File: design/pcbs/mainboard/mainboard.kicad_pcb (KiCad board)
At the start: 4 copper layers, 150 x 130 mm, 253 parts, among them J1 Conn_Coaxial, J10 Conn_01x04, J11 Conn_01x04, J15 Conn_01x01, J16 Conn_01x01, J17 Conn_01x01, J18 Conn_01x01, J2 Conn_Coaxial, J4 AudioJackSw, J5 Conn_01x03, K1 EC2-5NU, K2 EC2-5NU, K3 EC2-12NU, K4 EC2-12NU, Q1 SS8050, Q10 SS8050, Q11 SS8050, Q12 SS8050, Q2 SS8050, Q3 SS8050, Q4 SS8050, Q5 SS8550, Q6 SS8550, Q7 SS8050, Q8 SS8050, Q9 SS8050, U1 TPS79318-EP, U10 TPS7A49, U11 PCM1792A, U12 OPA1612AxD, U13 OPA1612AxD, U14 OPA1612AxD, U15 KC3225K24.5760C1GE00, U16 5PB1102, U17 STM8S003F3P, U18 Combo384, U19 TPS7A49, U2 SRC4392, U20 TPS7A30, U3 TLV1117-33, U4 TPS7A49, U5 TPS7A30, U6 Si8645BA-B-IU, U7 OPA1612AxD, U8 LME49600, U9 LME49600

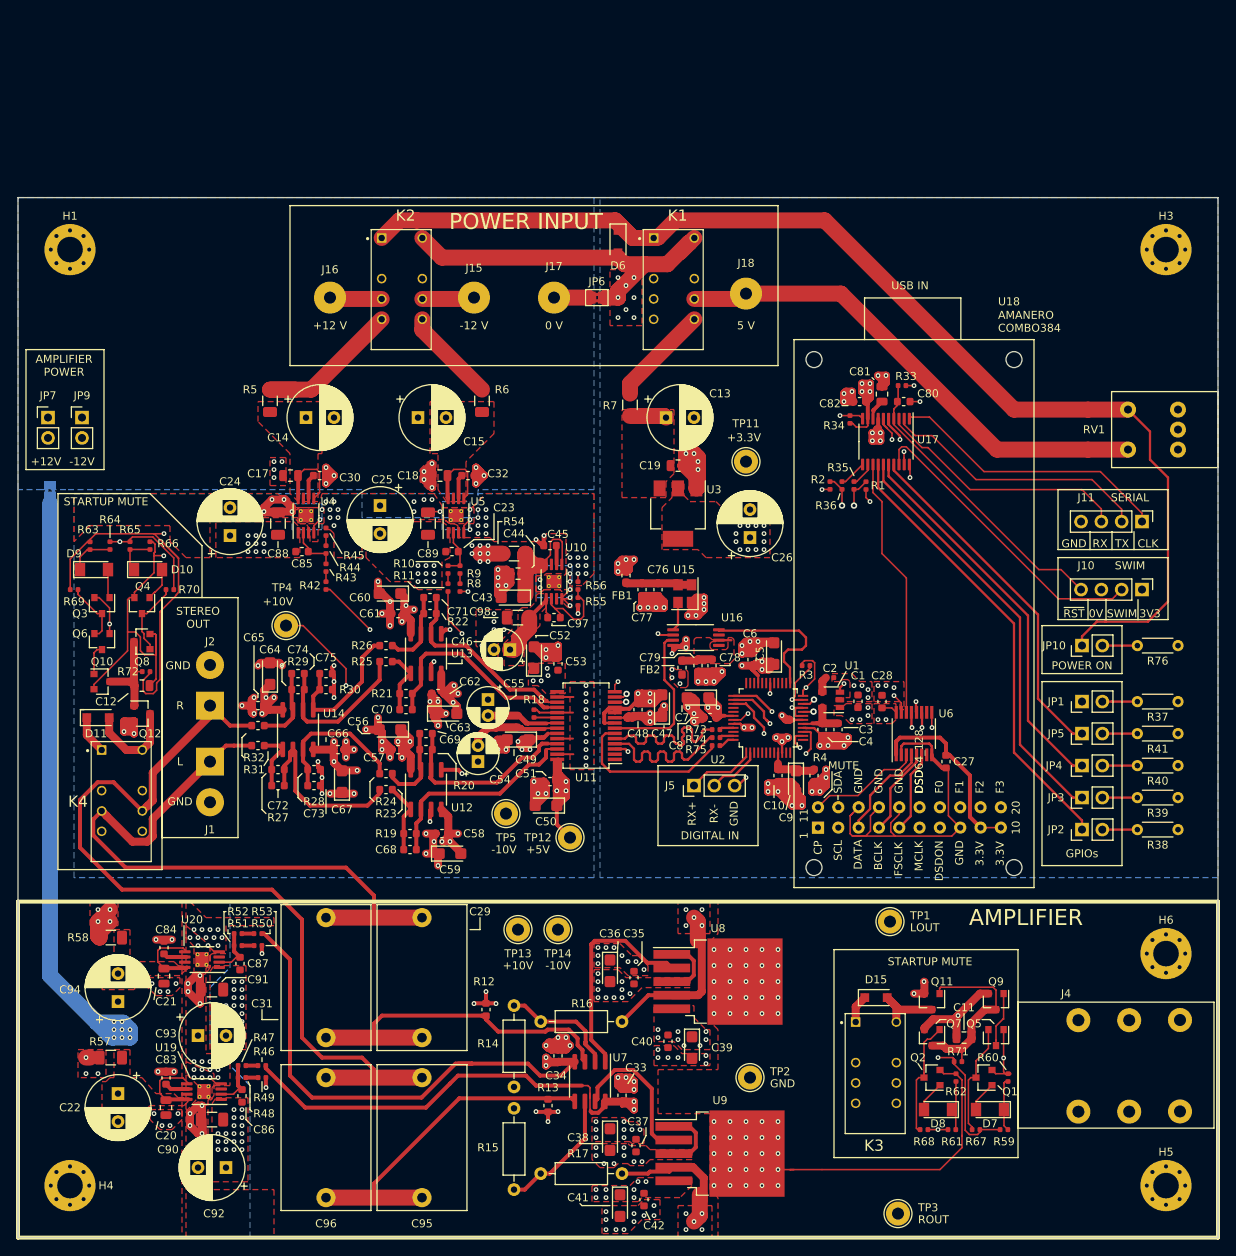
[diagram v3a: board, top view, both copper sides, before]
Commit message: Renumbered footprints to follow board position.
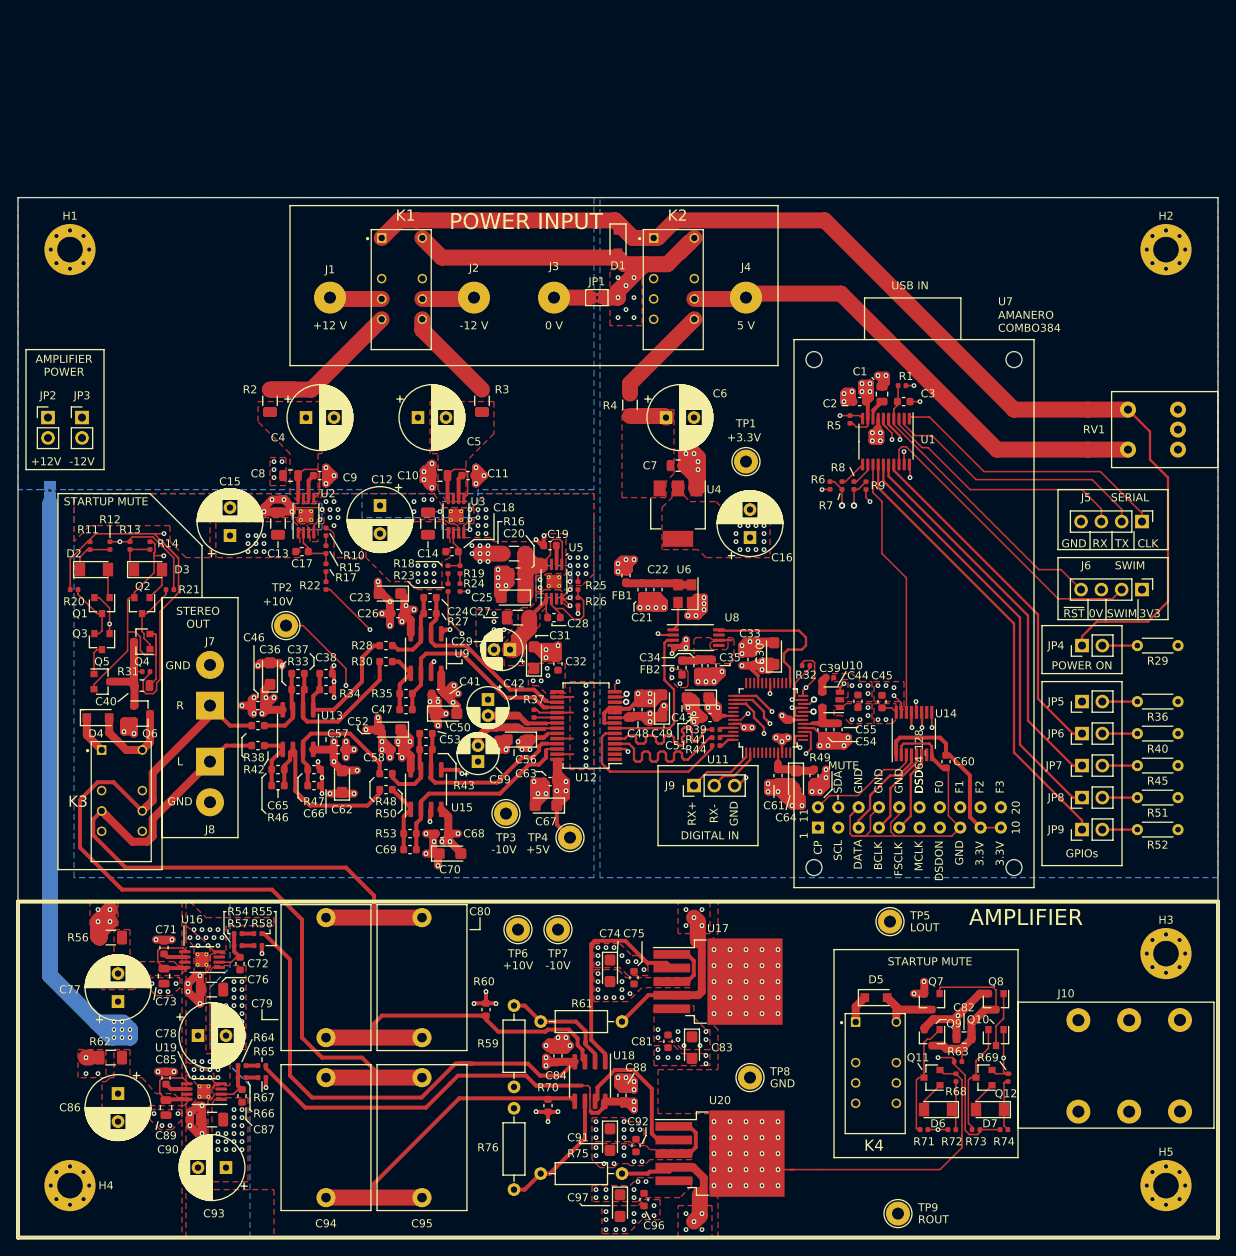
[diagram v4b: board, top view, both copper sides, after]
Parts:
- moved J4 0.50 mm to (81.0, 112.5)
- renumbered C81 to C1, C18 to C10, C32 to C11, C25 to C12, C88 to C13, C89 to C14, C24 to C15, C26 to C16, C85 to C17, C23 to C18, C45 to C19, C82 to C2, C44 to C20, C77 to C21, C76 to C22, C60 to C23, C71 to C24, C43 to C25, C61 to C26, C98 to C27, C97 to C28, C46 to C29, C80 to C3, C5 to C30, C52 to C31, C53 to C32, C6 to C33, C79 to C34, C78 to C35, C64 to C36, C74 to C37, C75 to C38, C2 to C39, C14 to C4, C12 to C40, C62 to C41, C55 to C42, C7 to C43, C1 to C44, C28 to C45, C65 to C46, C70 to C47, C47 to C49, C15 to C5, C63 to C50, C8 to C51, C56 to C52, C69 to C53, C4 to C54, C3 to C55, C49 to C56, C66 to C57, C57 to C58, C54 to C59, C13 to C6, C27 to C60, C10 to C61, C67 to C62, C51 to C63, C9 to C64, C72 to C65, C73 to C66, C50 to C67, C58 to C68, C68 to C69, C19 to C7, C59 to C70, C84 to C71, C87 to C72, C21 to C73, C36 to C74, C35 to C75, C91 to C76, C94 to C77, C93 to C78, C31 to C79, C17 to C8, C29 to C80, C40 to C81, C11 to C82, C39 to C83, C34 to C84, C83 to C85, C22 to C86, C86 to C87, C33 to C88, C20 to C89, C30 to C9, C38 to C91, C37 to C92, C92 to C93, C96 to C94, C42 to C96, C41 to C97, D6 to D1, D9 to D2, D10 to D3, D11 to D4, D15 to D5, D8 to D6, H3 to H2, H6 to H3, J16 to J1, J4 to J10, J15 to J2, J17 to J3, J18 to J4, J11 to J5, J10 to J6, J2 to J7, J1 to J8, J5 to J9, JP6 to JP1, JP8 to JP10, JP7 to JP2, JP9 to JP3, JP10 to JP4, JP1 to JP5, JP5 to JP6, JP4 to JP7, JP3 to JP8, JP2 to JP9, K2 to K1, K1 to K2, K4 to K3, K3 to K4, Q3 to Q1, Q5 to Q10, Q2 to Q11, Q1 to Q12, Q4 to Q2, Q6 to Q3, Q8 to Q4, Q10 to Q5, Q12 to Q6, Q11 to Q7, Q9 to Q8, Q7 to Q9, R33 to R1, R45 to R10, R63 to R11, R64 to R12, R65 to R13, R66 to R14, R44 to R15, R54 to R16, R43 to R17, R10 to R18, R9 to R19, R5 to R2, R69 to R20, R70 to R21, R42 to R22, R11 to R23, R8 to R24, R56 to R25, R55 to R26, R22 to R27, R26 to R28, R76 to R29, R6 to R3, R25 to R30, R72 to R31, R3 to R32, R29 to R33, R30 to R34, R21 to R35, R37 to R36, R18 to R37, R32 to R38, R73 to R39, R7 to R4, R41 to R40, R74 to R41, R31 to R42, R20 to R43, R75 to R44, R40 to R45, R27 to R46, R28 to R47, R24 to R48, R4 to R49, R34 to R5, R23 to R50, R39 to R51, R38 to R52, R19 to R53, R52 to R54, R53 to R55, R58 to R56, R51 to R57, R50 to R58, R14 to R59, R2 to R6, R12 to R60, R16 to R61, R57 to R62, R71 to R63, R47 to R64, R46 to R65, R48 to R66, R49 to R67, R62 to R68, R60 to R69, R36 to R7, R13 to R70, R68 to R71, R61 to R72, R67 to R73, R59 to R74, R17 to R75, R15 to R76, R35 to R8, R1 to R9, TP11 to TP1, TP4 to TP2, TP5 to TP3, TP12 to TP4, TP1 to TP5, TP13 to TP6, TP14 to TP7, TP2 to TP8, TP3 to TP9, U17 to U1, U1 to U10, U2 to U11, U11 to U12, U14 to U13, U6 to U14, U12 to U15, U20 to U16, U8 to U17, U7 to U18, U4 to U2, U9 to U20, U5 to U3, U3 to U4, U10 to U5, U15 to U6, U18 to U7, U16 to U8, U13 to U9
